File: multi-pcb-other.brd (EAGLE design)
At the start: 36.5 x 41.9 mm, 8 parts, among them Q1 BS170, X1 6B-ZR

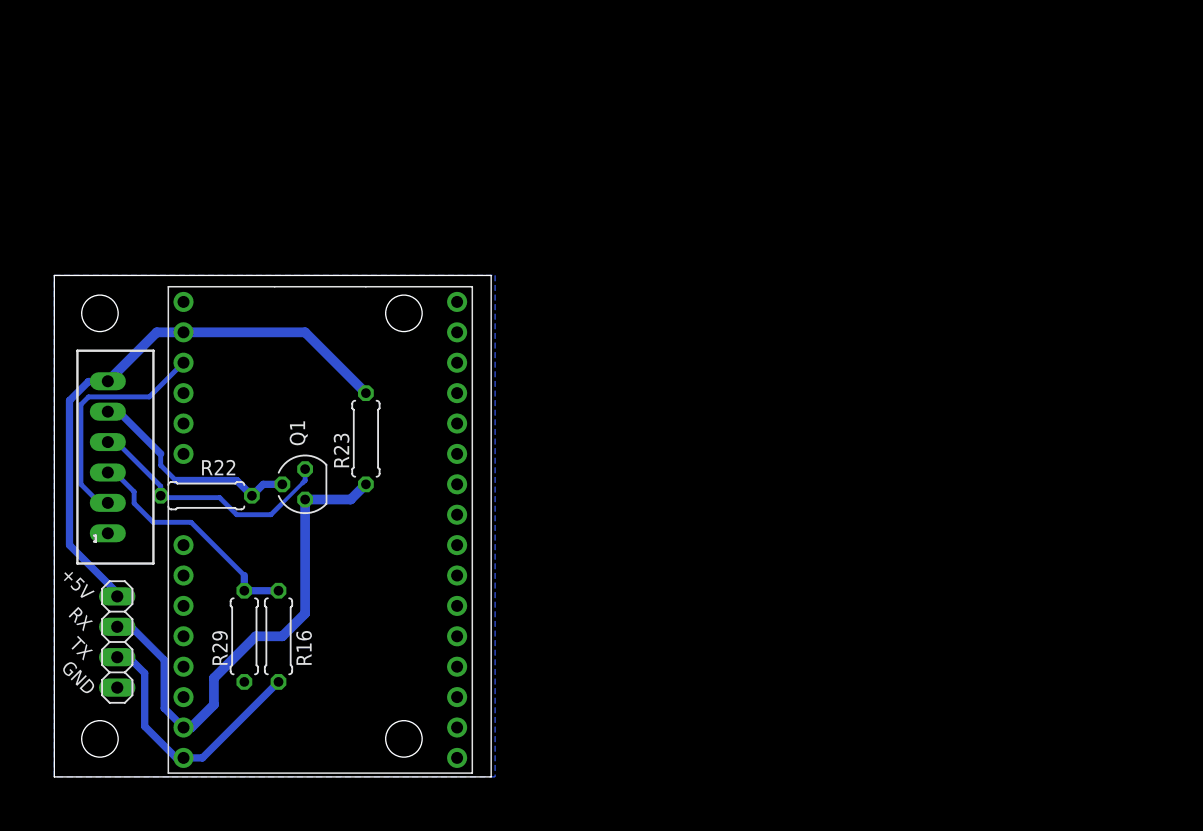
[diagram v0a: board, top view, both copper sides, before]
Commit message: Routed more multi-pcb boards
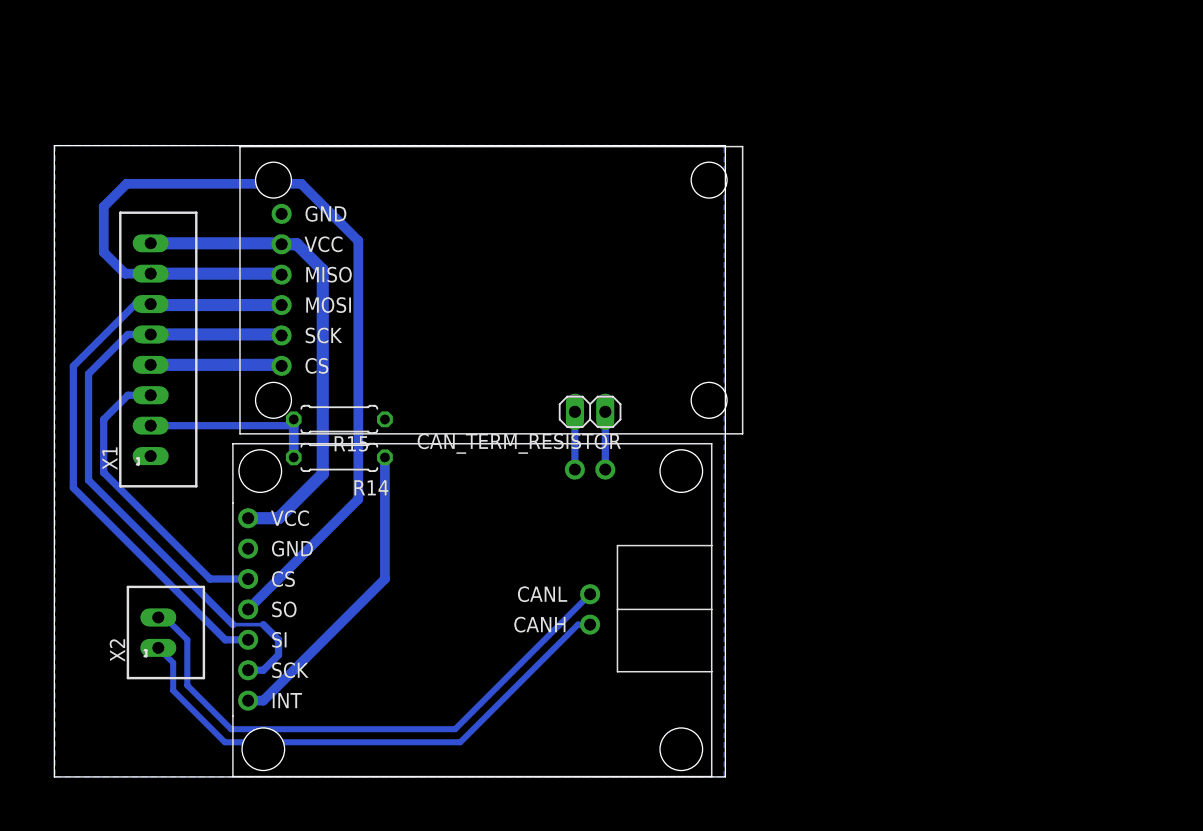
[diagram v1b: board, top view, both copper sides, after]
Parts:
- removed JP_UART2: (no value), pinhead:1X04
- removed Q1: BS170, transistor-small-signal:SOT54E
- removed R16: 5k, rcl:0207/7
- removed R22, R23, R29: 10k, rcl:0207/7
- removed U$6: A9G, A9:A9G
- added CAN_TERM_RESISTOR: (no value), pinhead:1X02
- added R14: 2k, rcl:0207/7
- added R15: 5k, rcl:0207/7
- added U$2: MCP2515_DEVBOARDINVERTED, MCP2515:MCP2515_DEVBOARD_INVERTED
- added U$5: HKD-MICRO-SD-BREAKOUTH, sd-mmc:HKD-MICRO-SD-BREAKOUT
- added X2: 2.52B-ZR, con-jst-custom:B2B-ZR2.5
- X1: value 6B-ZR -> 8B-ZR; device con-jst-custom:B6B-ZR2.5 -> con-jst-custom:B8B-ZR2.5
- moved X1 9.68 mm to (8.05, 35.7)
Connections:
- removed net +3V3: Q1.G, R22.2, X1.5
- removed net GPS_RX: JP_UART2.3, Q1.D, R23.1, U$6.IO0
- removed net GPS_TX: JP_UART2.2, R16.1, U$6.IO1
- removed net MCU_RESET: U$6.RST, X1.2
- removed net UART2_RX: R16.2, R29.2, X1.3
- removed net UART2_TX: Q1.S, R22.1, X1.4
- new net CAN_CS: U$2.CS, X1.3
- new net CAN_H: U$2.CAN_H, X2.1
- new net CAN_INT: R14.2, R15.2, X1.2
- new net CAN_L: U$2.CAN_L, X2.2
- new net CAN_TERM_RESTISTOR0: CAN_TERM_RESISTOR.2, U$2.TERM_REST0
- new net CAN_TERM_RESTISTOR1: CAN_TERM_RESISTOR.1, U$2.TERM_REST1
- new net N$10: R14.1, U$2.INT
- new net SD_CS: U$5.CS, X1.4
- new net SPI_MISO_5V: U$2.SO, U$5.MISO, X1.7
- new net SPI_MOSI: U$2.SI, U$5.MOSI, X1.6
- new net SPI_SCK: U$2.SCK, U$5.SCK, X1.5
- net +5V: now also U$2.VCC, U$5.VCC, X1.8; no longer JP_UART2.4, R23.2, U$6.5V, X1.6
- net GND: now also R15.1, U$2.GND, U$5.GND; no longer JP_UART2.1, R29.1, U$6.GND, U$6.GND2
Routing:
- net SPI_MISO_5V: track 0.00 -> 78.1 mm
- net SPI_SCK: track 0.00 -> 52.2 mm
- net SPI_MOSI: track 0.00 -> 49.6 mm
- net CAN_L: track 0.00 -> 46.9 mm
- net CAN_H: track 0.00 -> 44.8 mm
- net GPS_RX: track 41.9 -> 0.00 mm
- net N$10: track 0.00 -> 25.8 mm
- net CAN_CS: track 0.00 -> 25.0 mm
- net GPS_TX: track 22.2 -> 0.00 mm
- net UART2_TX: track 21.6 -> 0.00 mm
- net UART2_RX: track 19.7 -> 0.00 mm
- net MCU_RESET: track 19.6 -> 0.00 mm
- net +3V3: track 18.4 -> 0.00 mm
- net CAN_INT: track 0.00 -> 15.1 mm
- net SD_CS: track 0.00 -> 11.0 mm
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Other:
- board size 36.5 x 41.9 mm -> 56.1 x 52.7 mm
- board text removed: "+5V"
- board text removed: "GND"
- board text removed: "RX"
- board text removed: "TX"

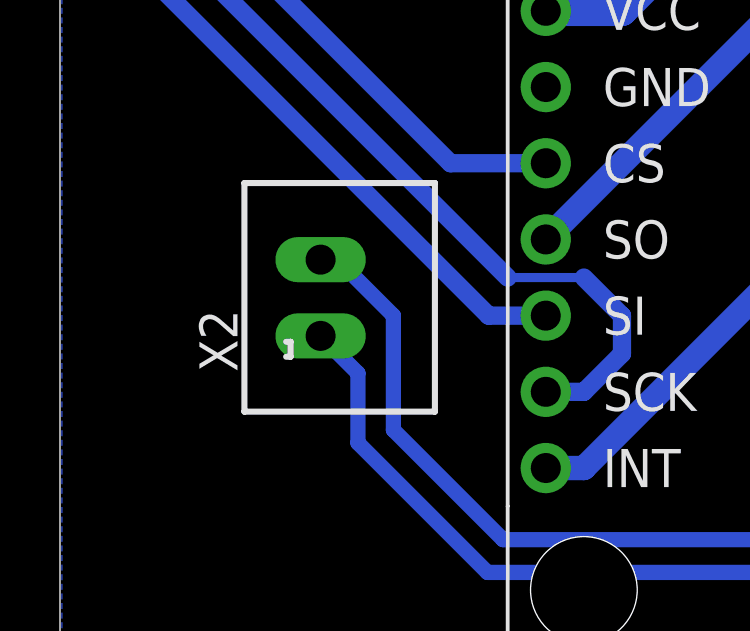
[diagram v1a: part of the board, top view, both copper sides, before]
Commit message: Fixed unalignment of connector
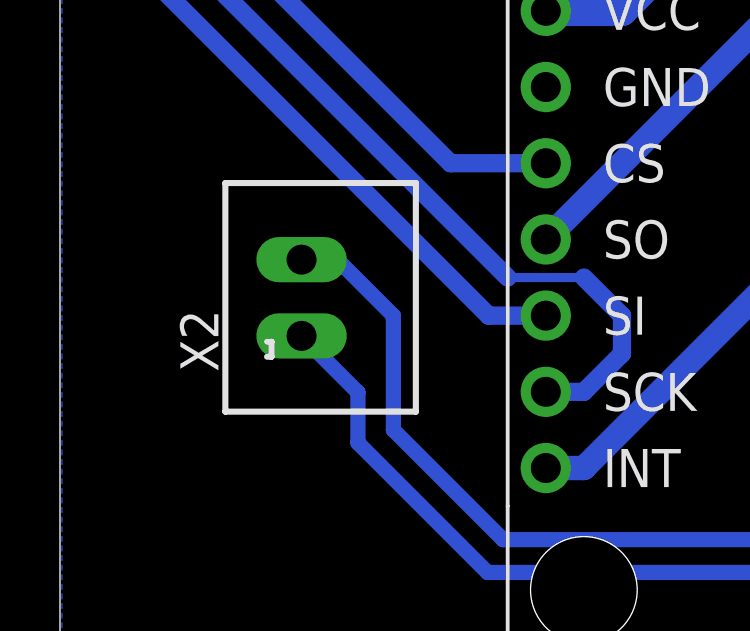
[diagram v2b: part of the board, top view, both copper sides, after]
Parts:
- moved X2 0.63 mm to (8.05, 12.1)
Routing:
- net CAN_L: track 46.9 -> 47.5 mm
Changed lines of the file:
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@@
 <setting verticaltext="up"/>
 </settings>
-<grid distance="12.5" unitdist="mil" unit="mil" style="lines" multiple="1" display="yes" altdistance="5" altunitdist="mil" altunit="mil"/>
+<grid distance="25" unitdist="mil" unit="mil" style="lines" multiple="1" display="yes" altdistance="5" altunitdist="mil" altunit="mil"/>
 <layers>
 <layer number="1" name="Top" color="4" fill="1" visible="yes" active="yes"/>
@@
 <attribute name="VALUE" x="14.0918" y="25.6124" size="1.27" layer="27" rot="R90"/>
 </element>
-<element name="X2" library="con-jst-custom" package="B2B-ZR2.5" value="2.52B-ZR" x="8.6868" y="12.065" smashed="yes" rot="R90">
-<attribute name="NAME" x="5.9168" y="9.585" size="1.27" layer="25" rot="R90"/>
-<attribute name="VALUE" x="14.7268" y="9.585" size="1.27" layer="27" rot="R90"/>
+<element name="X2" library="con-jst-custom" package="B2B-ZR2.5" value="2.52B-ZR" x="8.0518" y="12.065" smashed="yes" rot="R90">
+<attribute name="NAME" x="5.2818" y="9.585" size="1.27" layer="25" rot="R90"/>
+<attribute name="VALUE" x="14.0918" y="9.585" size="1.27" layer="27" rot="R90"/>
 </element>
 </elements>
@@
 <wire x1="43.7515" y1="12.7254" x2="33.9217" y2="2.8956" width="0.508" layer="16"/>
 <contactref element="X2" pad="1"/>
-<wire x1="9.9314" y1="9.5356" x2="8.6868" y2="10.7802" width="0.508" layer="16"/>
-<wire x1="9.9314" y1="7.2136" x2="9.9314" y2="9.5356" width="0.508" layer="16"/>
+<wire x1="9.9314" y1="8.9006" x2="8.0518" y2="10.7802" width="0.508" layer="16"/>
+<wire x1="9.9314" y1="7.2136" x2="9.9314" y2="8.9006" width="0.508" layer="16"/>
 </signal>
 <signal name="CAN_L">
@@
 <contactref element="X2" pad="2"/>
 <wire x1="11.1125" y1="11.4554" x2="9.2463" y2="13.3216" width="0.508" layer="16"/>
-<wire x1="8.6868" y1="13.3216" x2="9.2463" y2="13.3216" width="0.508" layer="16"/>
+<wire x1="8.0518" y1="13.3216" x2="9.2463" y2="13.3216" width="0.508" layer="16"/>
 </signal>
 <signal name="SD_CS">

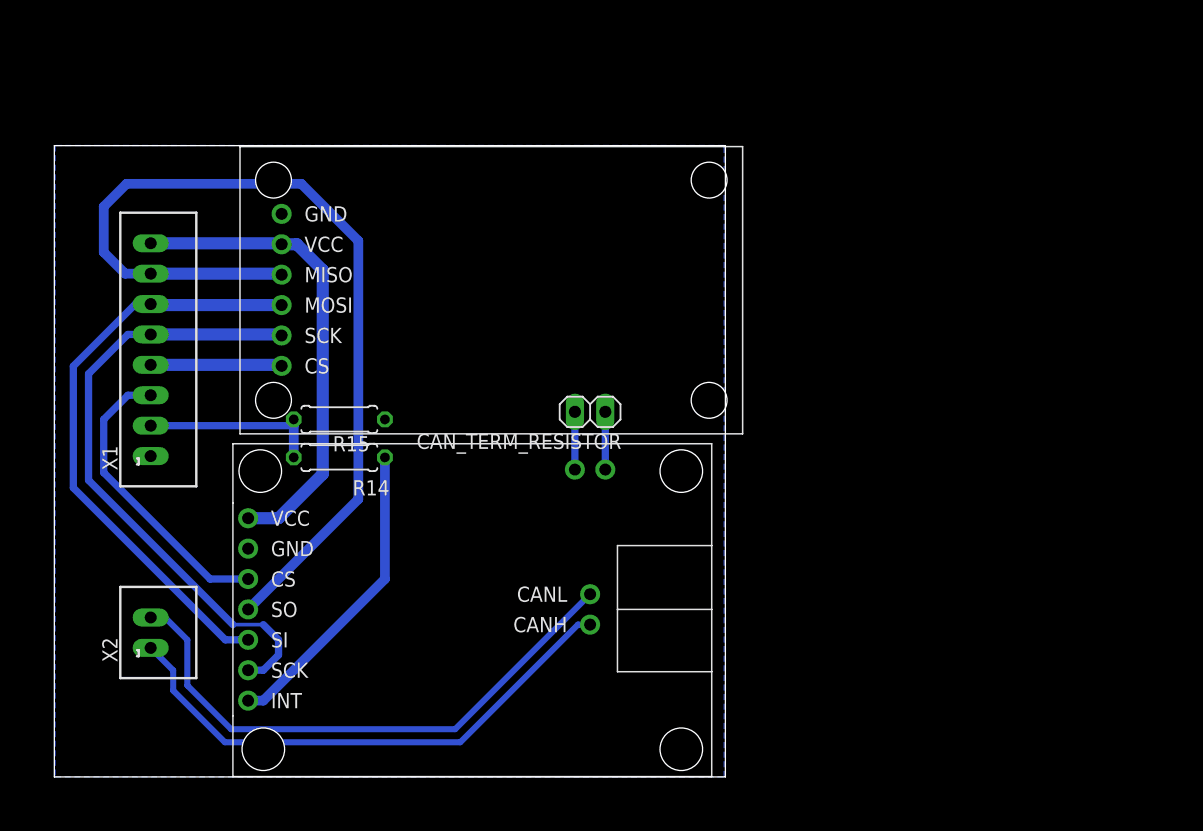
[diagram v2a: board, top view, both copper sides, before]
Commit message: Updated trace width and ground plane for others
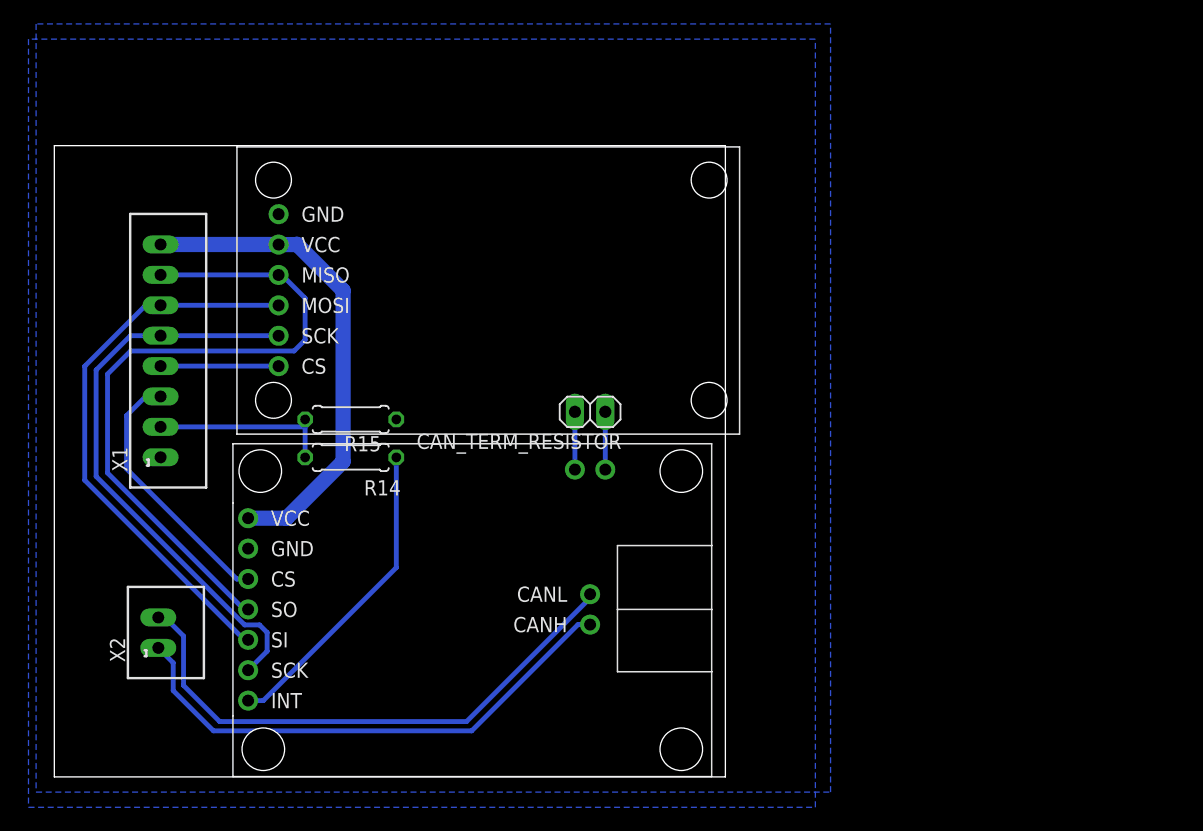
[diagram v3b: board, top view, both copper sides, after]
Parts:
- U$5: device sd-mmc:HKD-MICRO-SD-BREAKOUT -> samuel:HKD-MICRO-SD-BREAKOUT
- moved R14 0.95 mm to (24.8, 26.7)
- moved R15 0.95 mm to (24.8, 29.9)
- moved X1 0.83 mm to (8.88, 35.6)
- moved X2 0.63 mm to (8.69, 12.1)
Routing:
- net SPI_MISO_5V: track 78.1 -> 59.1 mm
- net SPI_SCK: track 52.2 -> 48.8 mm
- net CAN_CS: track 25.0 -> 21.9 mm
- net SPI_MOSI: track 49.6 -> 47.0 mm
- net SD_CS: track 11.0 -> 9.86 mm
- net CAN_H: track 45.0 -> 44.0 mm
- net +5V: track 40.1 -> 41.1 mm
- net CAN_L: track 47.5 -> 46.7 mm

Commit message: PCB layout for multi-pcb-other
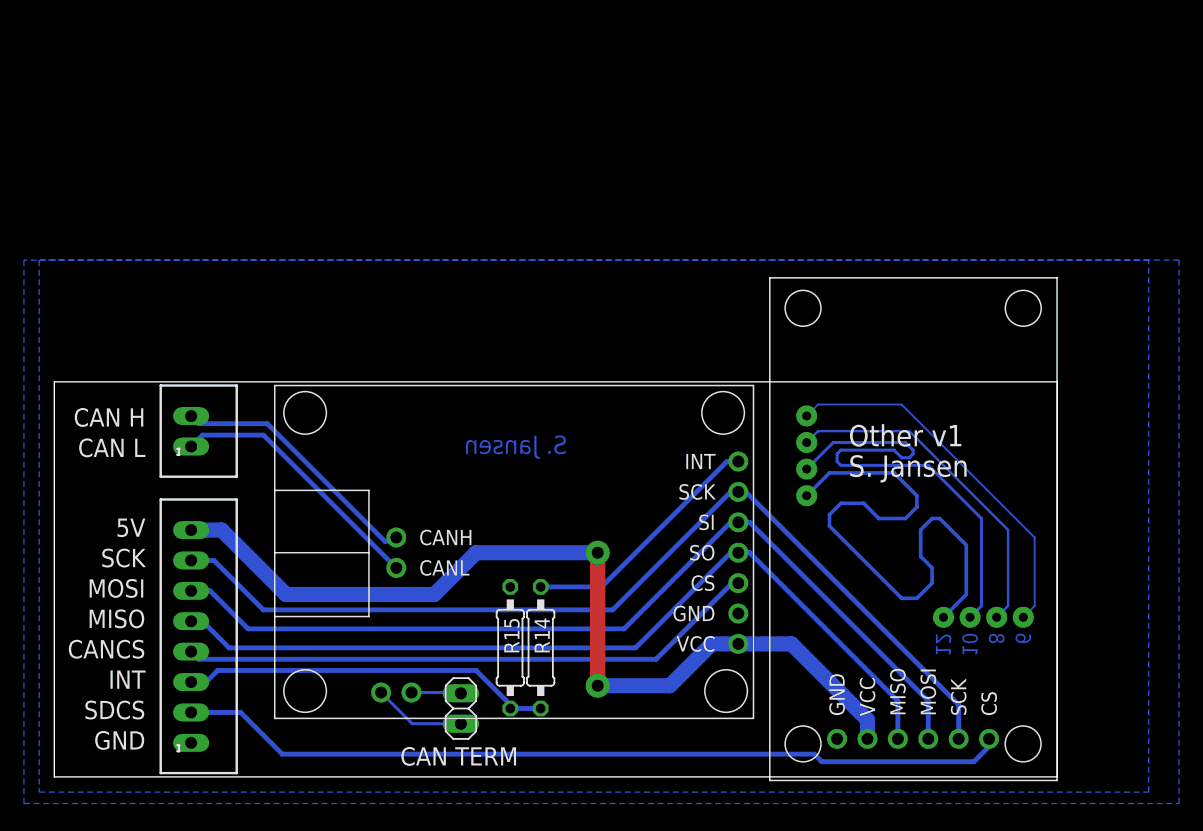
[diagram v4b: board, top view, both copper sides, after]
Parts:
- R14, R15: device rcl:0207/7 -> rcl:0207/10
- U$2: value MCP2515_DEVBOARDINVERTED -> MCP2515_DEVBOARDMCP2515_DEVBOARD_INVERTED_NODRILL; device MCP2515:MCP2515_DEVBOARD_INVERTED -> MCP2515:MCP2515_DEVBOARD_INVERTED_NODRILL
- U$5: value HKD-MICRO-SD-BREAKOUTH -> HKD-MICRO-SD-BREAKOUT; device samuel:HKD-MICRO-SD-BREAKOUT -> samuel:HKD-MICRO-SD-BREAKOUT_NODRILL
- moved U$5 40.4 mm to (71.8, 21.0), turned to 90 degrees
- moved CAN_TERM_RESISTOR 27.0 mm to (34.0, 5.71), turned to 90 degrees
- moved X1 24.0 mm to (11.4, 11.7)
- moved R15 23.3 mm to (38.1, 10.8), turned to 270 degrees
- moved R14 22.5 mm to (40.6, 10.8), turned to 270 degrees
- moved X2 17.0 mm to (11.4, 28.9)
- moved U$2 5.53 mm to (38.1, 18.7), turned to 180 degrees
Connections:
- net CAN_CS: now also X1.4; no longer X1.3
- net CAN_H: now also X2.2; no longer X2.1
- net CAN_INT: now also X1.3; no longer X1.2
- net CAN_L: now also X2.1; no longer X2.2
- net SD_CS: now also X1.2; no longer X1.4
- net SPI_MISO_5V: now also X1.5; no longer X1.7
- net SPI_SCK: now also X1.7; no longer X1.5
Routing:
- net SD_CS: track 9.86 -> 69.5 mm
- net N$4: track 0.00 -> 49.7 mm, vias 0 -> 2
- net N$1: track 0.00 -> 40.6 mm, vias 0 -> 2
- net +5V: track 41.1 -> 77.0 mm, vias 0 -> 2
- net SPI_SCK: track 48.8 -> 80.1 mm
- net N$3: track 0.00 -> 31.1 mm, vias 0 -> 2
- net SPI_MOSI: track 47.0 -> 76.0 mm
- net N$2: track 0.00 -> 28.3 mm, vias 0 -> 2
- net CAN_CS: track 21.9 -> 48.6 mm
- net CAN_L: track 46.7 -> 22.1 mm
- net CAN_H: track 44.0 -> 21.6 mm
- net CAN_INT: track 15.3 -> 31.1 mm
- net SPI_MISO_5V: track 59.1 -> 71.6 mm
- net N$10: track 26.2 -> 20.8 mm
- net CAN_TERM_RESTISTOR1: track 4.83 -> 7.75 mm
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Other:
- board size 56.1 x 52.7 mm -> 83.8 x 33 mm
- board text added: "10"
- board text added: "12"
- board text added: "5V"
- board text added: "6"
- board text added: "8"
- board text added: "CAN H"
- board text added: "CAN L"
- board text added: "CAN TERM"
- board text added: "CANCS"
- board text added: "GND"
- board text added: "INT"
- board text added: "MISO"
- board text added: "MOSI"
- board text added: "Other v1"
- board text added: "S. Jansen"
- board text added: "SCK"
- board text added: "SDCS"
